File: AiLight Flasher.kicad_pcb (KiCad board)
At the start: 2 copper layers, 28 x 28 mm, 8 parts, among them J1 GND, J2 IO0, J3 3V3, J4 aRX, J5 aTX, J6 FTDI

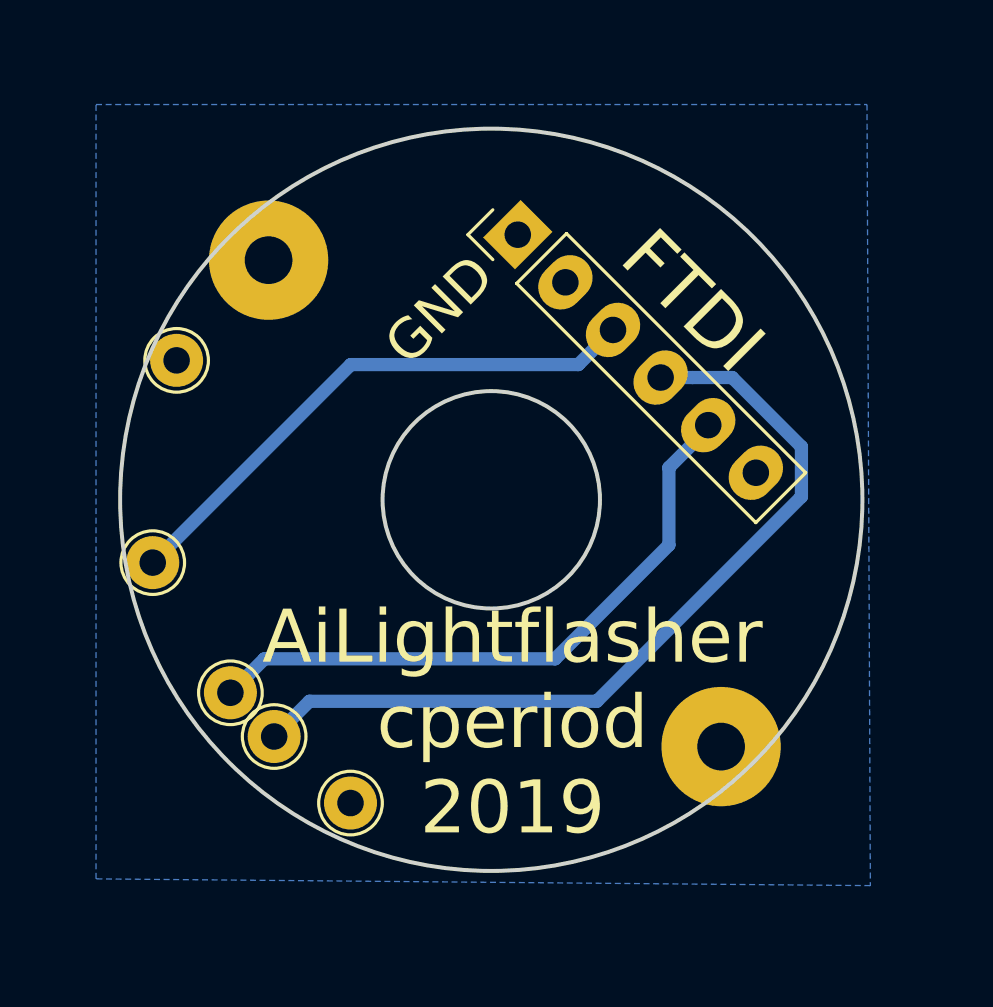
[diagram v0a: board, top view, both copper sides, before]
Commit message: add a jumper to IO0 so we can use the serial monitor to check if it flashed
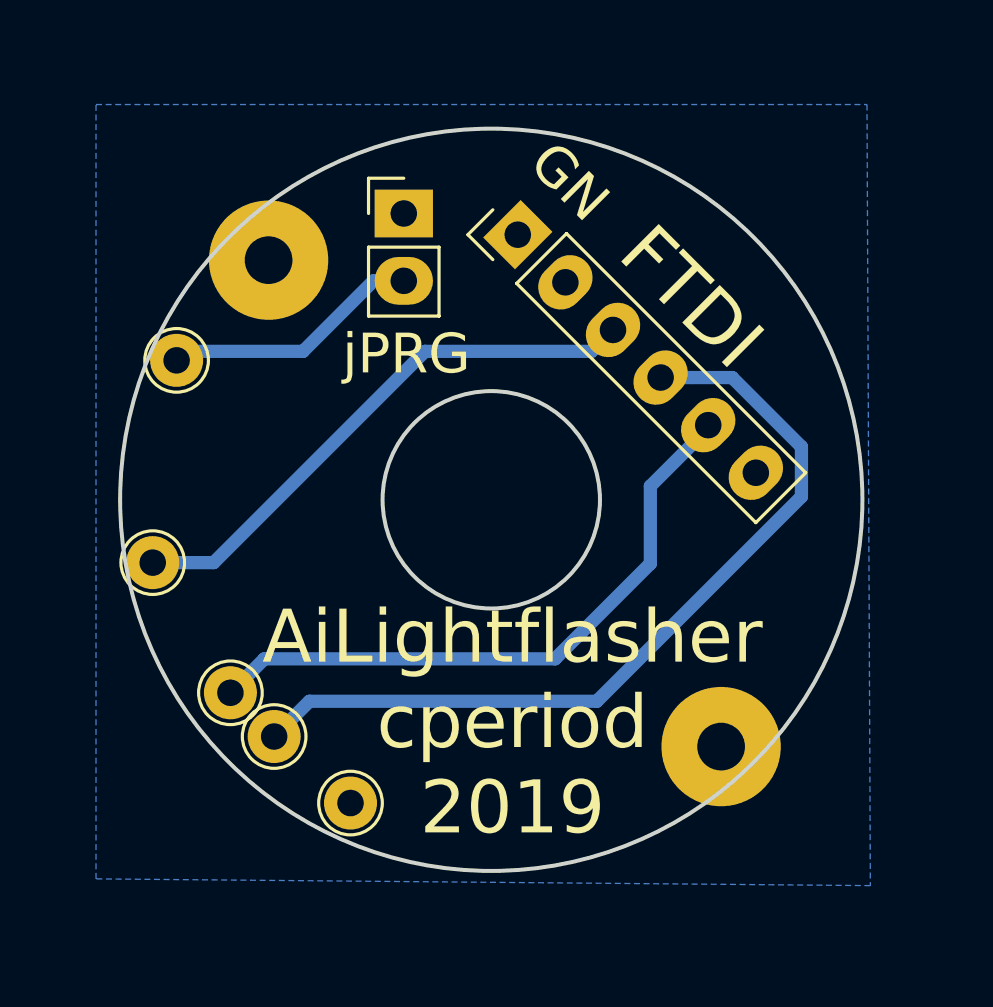
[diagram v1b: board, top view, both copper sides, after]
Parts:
- added JP1: Jumper, CPB:Socket_Strip_Straight_1x02_Oval_Pitch2.54mm, F.Cu at (96.7, 89.2)
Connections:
- J2 pad 1: GND -> Net-(J2-Pad1)
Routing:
- net Net-(J2-Pad1): track 0.00 -> 9.81 mm
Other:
- board text added: "GN"
- board text added: "jPRG"
- board text removed: "GND"
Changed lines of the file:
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@@
   (general
     (thickness 1.6)
-    (drawings 5)
-    (tracks 16)
+    (drawings 6)
+    (tracks 21)
     (zones 0)
-    (modules 8)
-    (nets 7)
+    (modules 9)
+    (nets 8)
   )
   (page A4)
@@
   (net 0 "")
   (net 1 GND)
-  (net 2 3V3)
-  (net 3 aRX)
-  (net 4 aTX)
-  (net 5 "Net-(J6-Pad6)")
-  (net 6 "Net-(J6-Pad2)")
+  (net 2 "Net-(J2-Pad1)")
+  (net 3 3V3)
+  (net 4 aRX)
+  (net 5 aTX)
+  (net 6 "Net-(J6-Pad6)")
+  (net 7 "Net-(J6-Pad2)")
   (net_class Default "This is the default net class."
     (clearance 0.2)
@@
     (add_net 3V3)
     (add_net GND)
+    (add_net "Net-(J2-Pad1)")
     (add_net "Net-(J6-Pad2)")
     (add_net "Net-(J6-Pad6)")
@@
     )
     (pad 1 thru_hole circle (at 0 0) (size 2 2) (drill 1) (layers *.Cu *.Mask)
-      (net 1 GND))
+      (net 2 "Net-(J2-Pad1)"))
   )
   (module CPB:Test_Point_THTPad_d2.0mm_Drill1.0mm (layer F.Cu)
@@
     (fp_circle (center 0 0) (end 0 1.2) (layer F.SilkS) (width 0.12))
     (pad 1 thru_hole circle (at 0 0) (size 2 2) (drill 1) (layers *.Cu *.Mask)
-      (net 2 3V3))
+      (net 3 3V3))
   )
   (module CPB:Test_Point_THTPad_d2.0mm_Drill1.0mm (layer F.Cu)
@@
     )
     (pad 1 thru_hole circle (at 0 0) (size 2 2) (drill 1) (layers *.Cu *.Mask)
-      (net 3 aRX))
+      (net 4 aRX))
   )
   (module CPB:Test_Point_THTPad_d2.0mm_Drill1.0mm (layer F.Cu)
@@
     (fp_circle (center 0 0) (end 0 1.2) (layer F.SilkS) (width 0.12))
     (pad 1 thru_hole circle (at 0 0) (size 2 2) (drill 1) (layers *.Cu *.Mask)
-      (net 4 aTX))
+      (net 5 aTX))
   )
   (module Wire_Pads:SolderWirePad_single_2mmDrill (layer F.Cu)
@@
       (effects (font (size 1 1) (thickness 0.15)))
     )
-    (fp_text value Align1 (at -0.635 3.81) (layer F.Fab)
+    (fp_text value Align1 (at -2.6 -2.96) (layer F.Fab)
       (effects (font (size 1 1) (thickness 0.15)))
     )
@@
       (effects (font (size 1 1) (thickness 0.15)))
     )
-    (fp_text value Align2 (at -0.635 3.81) (layer F.Fab)
+    (fp_text value Align2 (at 1.33 3.69) (layer F.Fab)
       (effects (font (size 1 1) (thickness 0.15)))
     )
@@
       (net 1 GND))
     (pad 2 thru_hole oval (at 0 2.54 45) (size 2.2 1.7) (drill 1) (layers *.Cu *.Mask)
-      (net 6 "Net-(J6-Pad2)"))
+      (net 7 "Net-(J6-Pad2)"))
     (pad 3 thru_hole oval (at 0 5.08 45) (size 2.2 1.7) (drill 1) (layers *.Cu *.Mask)
-      (net 2 3V3))
+      (net 3 3V3))
     (pad 4 thru_hole oval (at 0 7.62 45) (size 2.2 1.7) (drill 1) (layers *.Cu *.Mask)
-      (net 3 aRX))
+      (net 4 aRX))
     (pad 5 thru_hole oval (at 0 10.16 45) (size 2.2 1.7) (drill 1) (layers *.Cu *.Mask)
-      (net 4 aTX))
+      (net 5 aTX))
     (pad 6 thru_hole oval (at 0 12.7 45) (size 2.2 1.7) (drill 1) (layers *.Cu *.Mask)
-      (net 5 "Net-(J6-Pad6)"))
+      (net 6 "Net-(J6-Pad6)"))
     (model ${KISYS3DMOD}/Socket_Strips.3dshapes/Socket_Strip_Straight_1x06_Pitch2.54mm.wrl
       (offset (xyz 0 -6.349999904632568 0))
@@
     )
   )
-  (gr_text FTDI (at 107.6 92.5 315) (layer F.SilkS)
+  (module CPB:Socket_Strip_Straight_1x02_Oval_Pitch2.54mm (layer F.Cu)
+    (at 96.7 89.2)
+    (descr "Through hole straight socket strip, 1x02, 2.54mm pitch, single row")
+    (tags "Through hole socket strip THT 1x02 2.54mm single row")
+    (fp_text reference JP1 (at 0 -2.33) (layer F.SilkS) hide
+      (effects (font (size 1 1) (thickness 0.15)))
+    )
+    (fp_text value Jumper (at 0 4.87) (layer F.Fab)
+      (effects (font (size 1 1) (thickness 0.15)))
+    )
+    (fp_text user %R (at 0 -2.33) (layer F.Fab)
+      (effects (font (size 1 1) (thickness 0.15)))
+    )
+    (fp_line (start 1.8 -1.8) (end -1.8 -1.8) (layer F.CrtYd) (width 0.05))
+    (fp_line (start 1.8 4.35) (end 1.8 -1.8) (layer F.CrtYd) (width 0.05))
+    (fp_line (start -1.8 4.35) (end 1.8 4.35) (layer F.CrtYd) (width 0.05))
+    (fp_line (start -1.8 -1.8) (end -1.8 4.35) (layer F.CrtYd) (width 0.05))
+    (fp_line (start -1.33 -1.33) (end 0 -1.33) (layer F.SilkS) (width 0.12))
+    (fp_line (start -1.33 0) (end -1.33 -1.33) (layer F.SilkS) (width 0.12))
+    (fp_line (start 1.33 1.27) (end -1.33 1.27) (layer F.SilkS) (width 0.12))
+    (fp_line (start 1.33 3.87) (end 1.33 1.27) (layer F.SilkS) (width 0.12))
+    (fp_line (start -1.33 3.87) (end 1.33 3.87) (layer F.SilkS) (width 0.12))
+    (fp_line (start -1.33 1.27) (end -1.33 3.87) (layer F.SilkS) (width 0.12))
+    (fp_line (start 1.27 -1.27) (end -1.27 -1.27) (layer F.Fab) (width 0.1))
+    (fp_line (start 1.27 3.81) (end 1.27 -1.27) (layer F.Fab) (width 0.1))
+    (fp_line (start -1.27 3.81) (end 1.27 3.81) (layer F.Fab) (width 0.1))
+    (fp_line (start -1.27 -1.27) (end -1.27 3.81) (layer F.Fab) (width 0.1))
+    (pad 2 thru_hole oval (at 0 2.54) (size 2.2 1.8) (drill 1) (layers *.Cu *.Mask)
+      (net 2 "Net-(J2-Pad1)"))
+    (pad 1 thru_hole rect (at 0 0) (size 2.2 1.8) (drill 1) (layers *.Cu *.Mask)
+      (net 1 GND))
+    (model ${KISYS3DMOD}/Socket_Strips.3dshapes/Socket_Strip_Straight_1x02_Pitch2.54mm.wrl
+      (offset (xyz 0 -1.269999980926514 0))
+      (scale (xyz 1 1 1))
+      (rotate (xyz 0 0 270))
+    )
+  )
+  (gr_text jPRG (at 96.8 94.5) (layer F.SilkS)
+    (effects (font (size 1.5 1.5) (thickness 0.3)))
+  )
+  (gr_text FTDI (at 107.55 92.35 315) (layer F.SilkS)
     (effects (font (size 2 2) (thickness 0.3)))
   )
@@
     (effects (font (size 2 2) (thickness 0.3)))
   )
-  (gr_text GND (at 98.044 92.837 45) (layer F.SilkS)
+  (gr_text GN (at 102.95 88 315) (layer F.SilkS)
     (effects (font (size 1.5 1.5) (thickness 0.3)))
   )
   (gr_circle (center 100 100) (end 104.1 100) (layer Edge.Cuts) (width 0.15))
   (gr_circle (center 100 100) (end 114 100) (layer Edge.Cuts) (width 0.15))
-  (segment (start 103.284204 94.9) (end 104.592102 93.592102) (width 0.5) (layer B.Cu) (net 2))
-  (segment (start 87.23 102.37) (end 94.7 94.9) (width 0.5) (layer B.Cu) (net 2))
-  (segment (start 94.7 94.9) (end 103.284204 94.9) (width 0.5) (layer B.Cu) (net 2))
-  (segment (start 93.14 107.6) (end 103.982 107.6) (width 0.5) (layer B.Cu) (net 3))
-  (segment (start 103.982 107.6) (end 111.7 99.882) (width 0.5) (layer B.Cu) (net 3))
-  (segment (start 107.590235 95.388154) (end 106.388154 95.388154) (width 0.5) (layer B.Cu) (net 3))
-  (segment (start 111.7 98) (end 109.088154 95.388154) (width 0.5) (layer B.Cu) (net 3))
-  (segment (start 111.7 99.882) (end 111.7 98) (width 0.5) (layer B.Cu) (net 3))
-  (segment (start 91.81 108.93) (end 93.14 107.6) (width 0.5) (layer B.Cu) (net 3))
-  (segment (start 109.088154 95.388154) (end 107.590235 95.388154) (width 0.5) (layer B.Cu) (net 3))
-  (segment (start 106.7 98.786) (end 108.184205 97.301795) (width 0.5) (layer B.Cu) (net 4))
-  (segment (start 108.184205 97.301795) (end 108.184205 97.184205) (width 0.5) (layer B.Cu) (net 4))
-  (segment (start 106.7 101.707) (end 106.7 98.786) (width 0.5) (layer B.Cu) (net 4))
-  (segment (start 102.407 106) (end 106.7 101.707) (width 0.5) (layer B.Cu) (net 4))
-  (segment (start 90.16 107.28) (end 91.44 106) (width 0.5) (layer B.Cu) (net 4))
-  (segment (start 91.44 106) (end 102.407 106) (width 0.5) (layer B.Cu) (net 4))
+  (segment (start 95.56 91.74) (end 96.7 91.74) (width 0.5) (layer B.Cu) (net 2))
+  (segment (start 92.9 94.4) (end 95.56 91.74) (width 0.5) (layer B.Cu) (net 2))
+  (segment (start 88.13 94.74) (end 88.47 94.4) (width 0.5) (layer B.Cu) (net 2))
+  (segment (start 88.47 94.4) (end 92.9 94.4) (width 0.5) (layer B.Cu) (net 2))
+  (segment (start 103.784204 94.4) (end 104.592102 93.592102) (width 0.5) (layer B.Cu) (net 3))
+  (segment (start 97.5 94.4) (end 103.784204 94.4) (width 0.5) (layer B.Cu) (net 3))
+  (segment (start 87.23 102.37) (end 89.53 102.37) (width 0.5) (layer B.Cu) (net 3))
+  (segment (start 89.53 102.37) (end 97.5 94.4) (width 0.5) (layer B.Cu) (net 3))
+  (segment (start 93.14 107.6) (end 103.982 107.6) (width 0.5) (layer B.Cu) (net 4))
+  (segment (start 103.982 107.6) (end 111.7 99.882) (width 0.5) (layer B.Cu) (net 4))
+  (segment (start 107.590235 95.388154) (end 106.388154 95.388154) (width 0.5) (layer B.Cu) (net 4))
+  (segment (start 111.7 98) (end 109.088154 95.388154) (width 0.5) (layer B.Cu) (net 4))
+  (segment (start 111.7 99.882) (end 111.7 98) (width 0.5) (layer B.Cu) (net 4))
+  (segment (start 91.81 108.93) (end 93.14 107.6) (width 0.5) (layer B.Cu) (net 4))
+  (segment (start 109.088154 95.388154) (end 107.590235 95.388154) (width 0.5) (layer B.Cu) (net 4))
+  (segment (start 106 99.486) (end 108.184205 97.301795) (width 0.5) (layer B.Cu) (net 5))
+  (segment (start 106 102.407) (end 106 99.486) (width 0.5) (layer B.Cu) (net 5))
+  (segment (start 108.184205 97.301795) (end 108.184205 97.184205) (width 0.5) (layer B.Cu) (net 5))
+  (segment (start 102.407 106) (end 106 102.407) (width 0.5) (layer B.Cu) (net 5))
+  (segment (start 90.16 107.28) (end 91.44 106) (width 0.5) (layer B.Cu) (net 5))
+  (segment (start 91.44 106) (end 102.407 106) (width 0.5) (layer B.Cu) (net 5))
   (zone (net 1) (net_name GND) (layer B.Cu) (hatch edge 0.508)
     (connect_pads (clearance 0.6))

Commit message: bump the size slightly, flip the FTDI header around to give more space
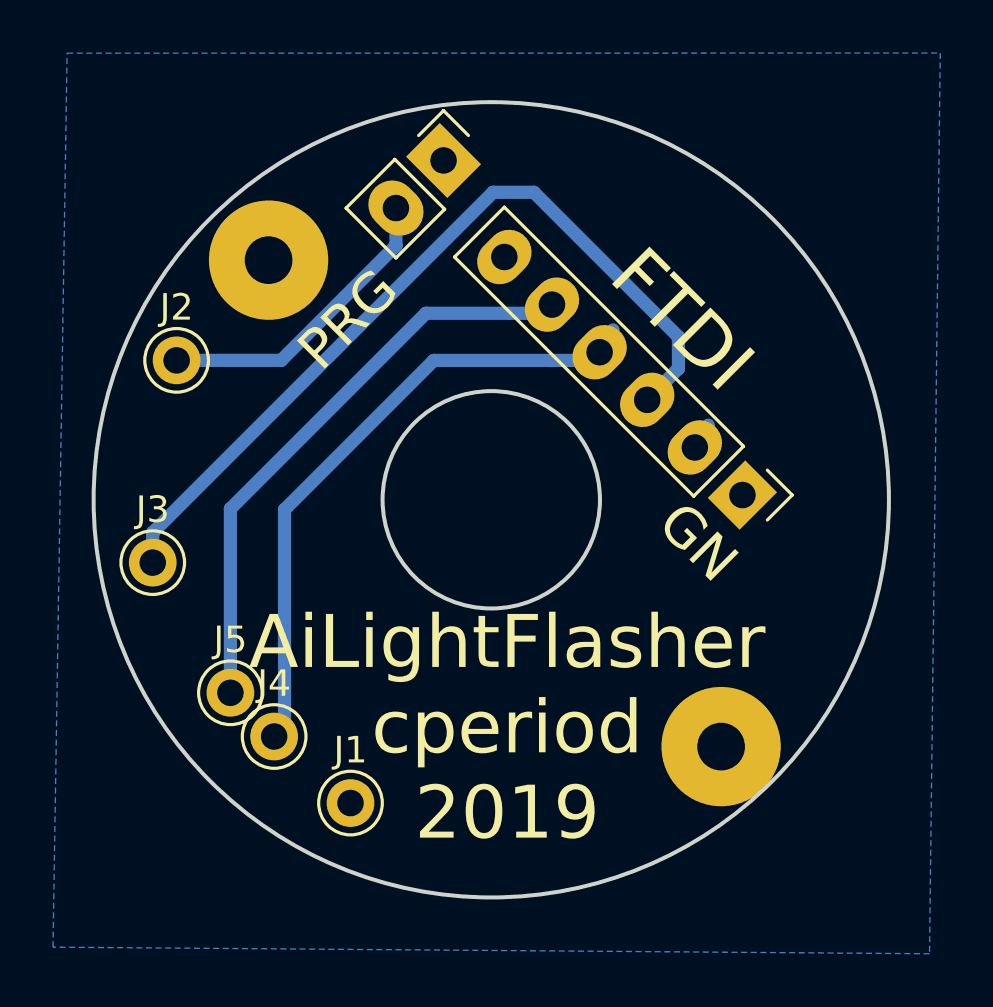
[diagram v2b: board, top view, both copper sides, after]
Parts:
- moved J6 13.0 mm to (109.5, 99.8), turned to 225 degrees
- moved JP1 2.50 mm to (98.2, 87.2), turned to 315 degrees
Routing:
- net 3V3: track 21.0 -> 31.4 mm
- net aRX: track 31.9 -> 24.2 mm
- net Net-(J2-Pad1): track 9.81 -> 12.0 mm
- net aTX: track 24.0 -> 22.3 mm
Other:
- board size 28 x 28 mm -> 30 x 30 mm
- board text added: "AiLightFlasher cperiod 2019"
- board text added: "PRG"
- board text removed: "AiLightflasher cperiod 2019"
- board text removed: "jPRG"
